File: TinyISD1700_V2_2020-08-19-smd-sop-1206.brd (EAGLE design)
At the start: 45.5 x 48.3 mm, 18 parts, among them IC3 LM317MDT, U1 ATTINY4313-SU

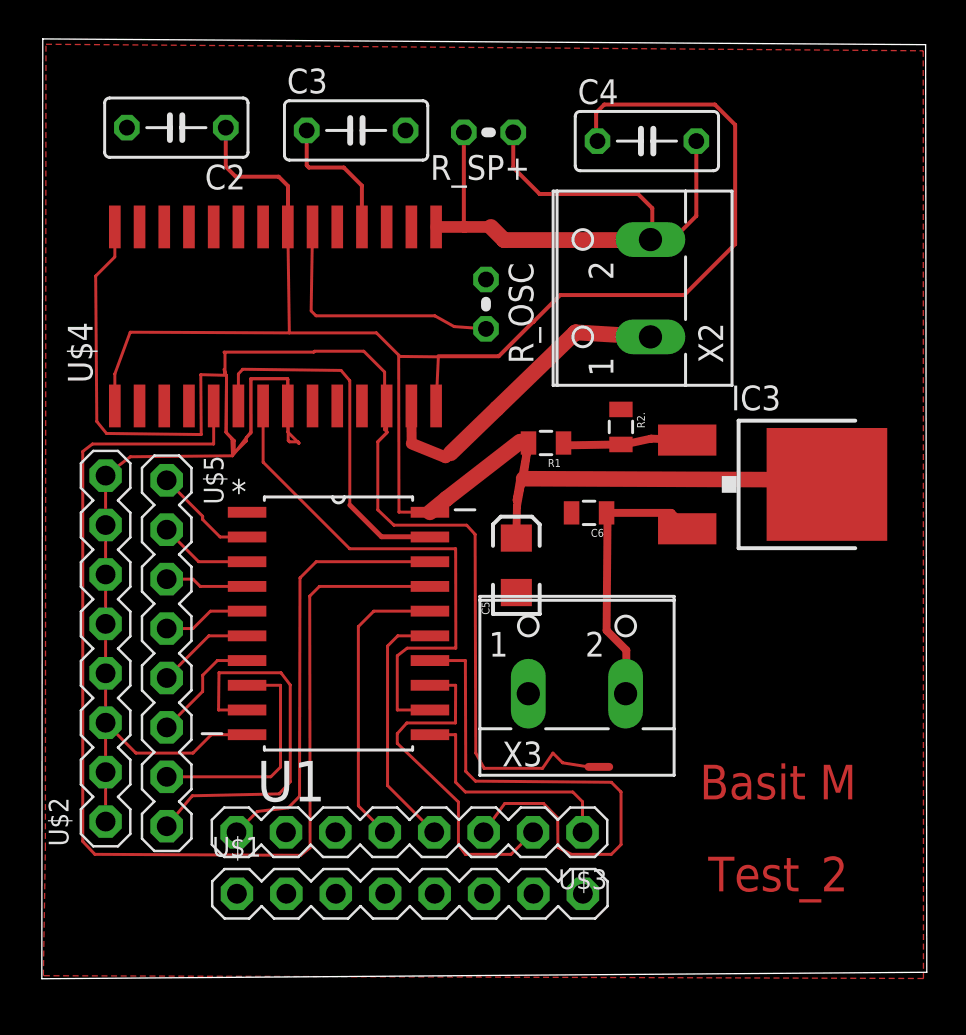
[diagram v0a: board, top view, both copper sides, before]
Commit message: resized board
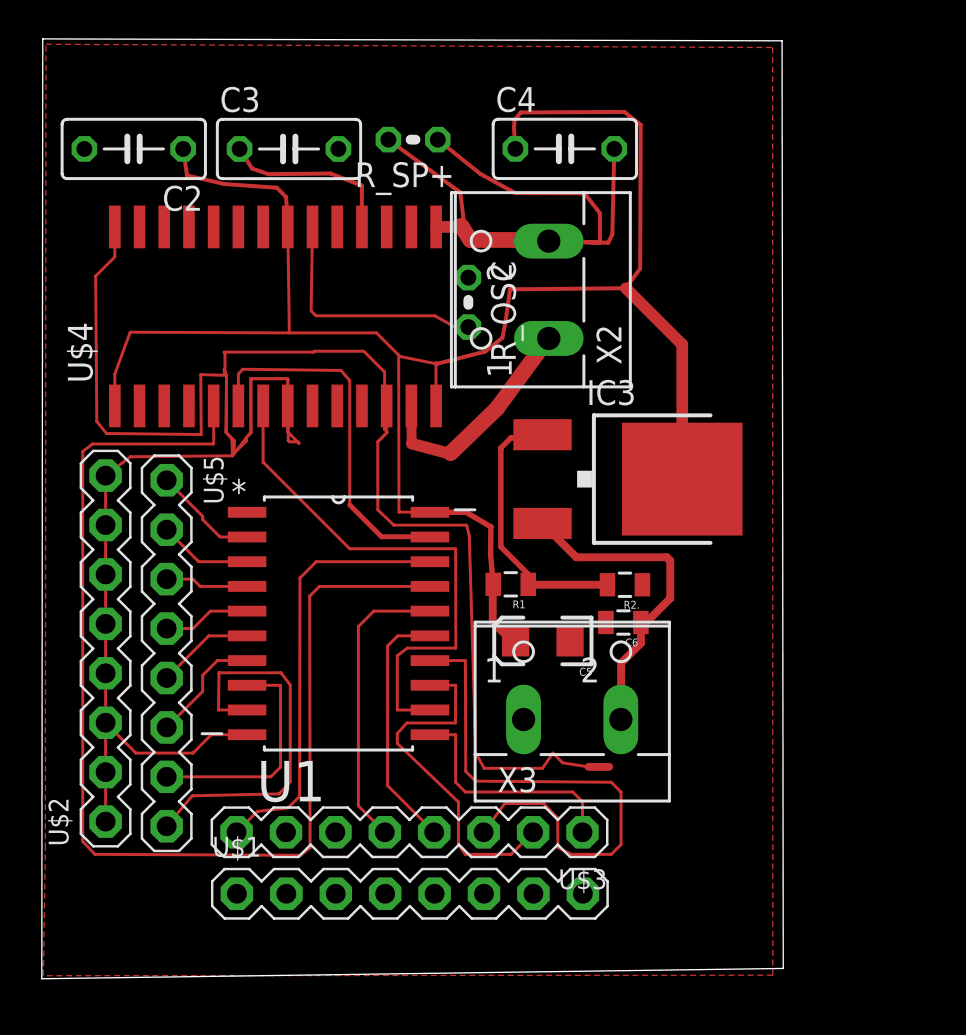
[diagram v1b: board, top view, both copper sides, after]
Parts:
- moved R2. 8.11 mm to (28.0, 17.1), turned to 180 degrees
- moved R1 7.49 mm to (22.1, 17.1)
- moved IC3 7.44 mm to (28.6, 22.5)
- moved C6 5.90 mm to (27.9, 15.1)
- moved X2 5.23 mm to (22.8, 32.2)
- moved C4 4.24 mm to (24.9, 39.5)
- moved C5 4.12 mm to (23.8, 14.2), turned to 180 degrees
- moved R_SP+ 3.90 mm to (17.1, 39.9)
- moved C3 3.58 mm to (10.7, 39.5)
- moved C2 2.45 mm to (2.75, 39.5)
- moved X3 1.35 mm to (25.3, 11.4)
- moved R_OSC 0.91 mm to (19.9, 31.6)
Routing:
- net VCC: track 111.5 -> 95.9 mm
- net N$29: track 6.42 -> 14.1 mm
- net N$6: track 16.9 -> 11.8 mm
- net N$4: track 18.2 -> 21.8 mm
- net N$7: track 16.1 -> 13.0 mm
- net N$28: track 14.3 -> 16.9 mm
- net N$5: track 7.18 -> 9.12 mm
- net N$1: track 13.6 -> 12.6 mm
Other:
- board size 45.5 x 48.3 mm -> 38.1 x 48.3 mm
- board text removed: "Basit M"
- board text removed: "Test_2"

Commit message: commit
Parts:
- added J1: AVR_SPI_PRG_6OFFSET_PADS, SparkFun:2X3_OFFSET
- added JP1: (no value), jumper:JP1
- moved R_SP+ 0.74 mm to (17.8, 39.6)
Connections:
- new net ANALN: J1.5, U$4.9, U1.1
- new net MISO: J1.1
- new net N$19: C5.A, IC3.4, JP1.2, R1.2
- net CSK: now also J1.3
- net GND: now also J1.6
- net MOSI: now also J1.4
- net VCC: now also J1.2, JP1.1; no longer C5.A, IC3.4, R1.2
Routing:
- net GND: track 125.7 -> 213.6 mm
- net N$19: track 0.00 -> 29.4 mm
- net VCC: track 95.9 -> 80.5 mm
- net ANALN: track 0.00 -> 8.61 mm
- net SS: track 27.3 -> 32.7 mm
- net CSK: track 18.9 -> 21.1 mm
- net N$3: track 28.5 -> 27.8 mm
- net N$7: track 13.0 -> 12.3 mm
- net N$4: track 21.8 -> 21.1 mm
- net N$1: track 12.6 -> 12.1 mm
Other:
- board size 38.1 x 48.3 mm -> 41.7 x 48.9 mm
- board text added: "CSK"
- board text added: "GND"
- board text added: "MISO"
- board text added: "MOSI"
- board text added: "RESET"
- board text added: "vcc"
